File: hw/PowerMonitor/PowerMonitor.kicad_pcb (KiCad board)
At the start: 2 copper layers, 100 x 100 mm, 10 parts, among them J1 Conn_01x02_Socket, J2 Conn_01x02_Socket, J3 Conn_01x02_Socket, J4 Conn_01x02_Socket, J5 Conn_01x02_Socket

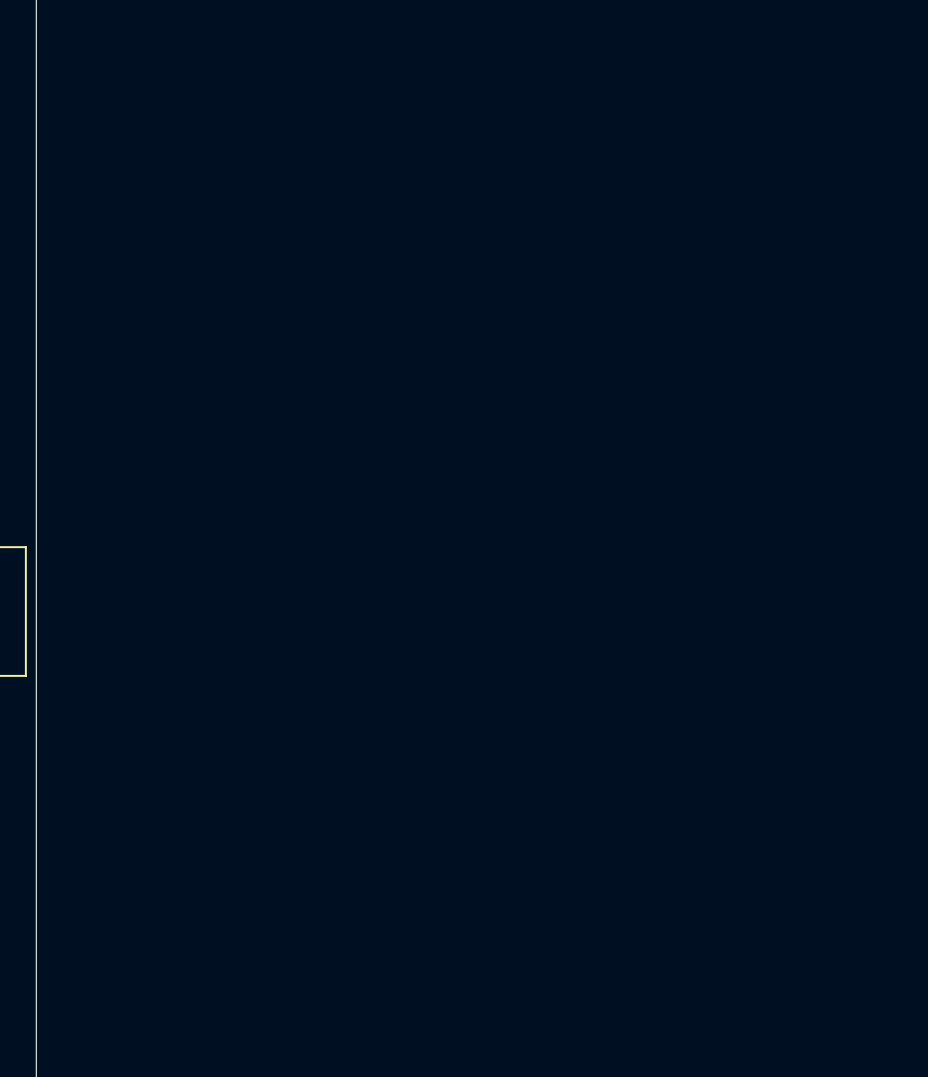
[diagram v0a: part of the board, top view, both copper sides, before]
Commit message: preliminar design for battery power monitor, add sd card to fmu
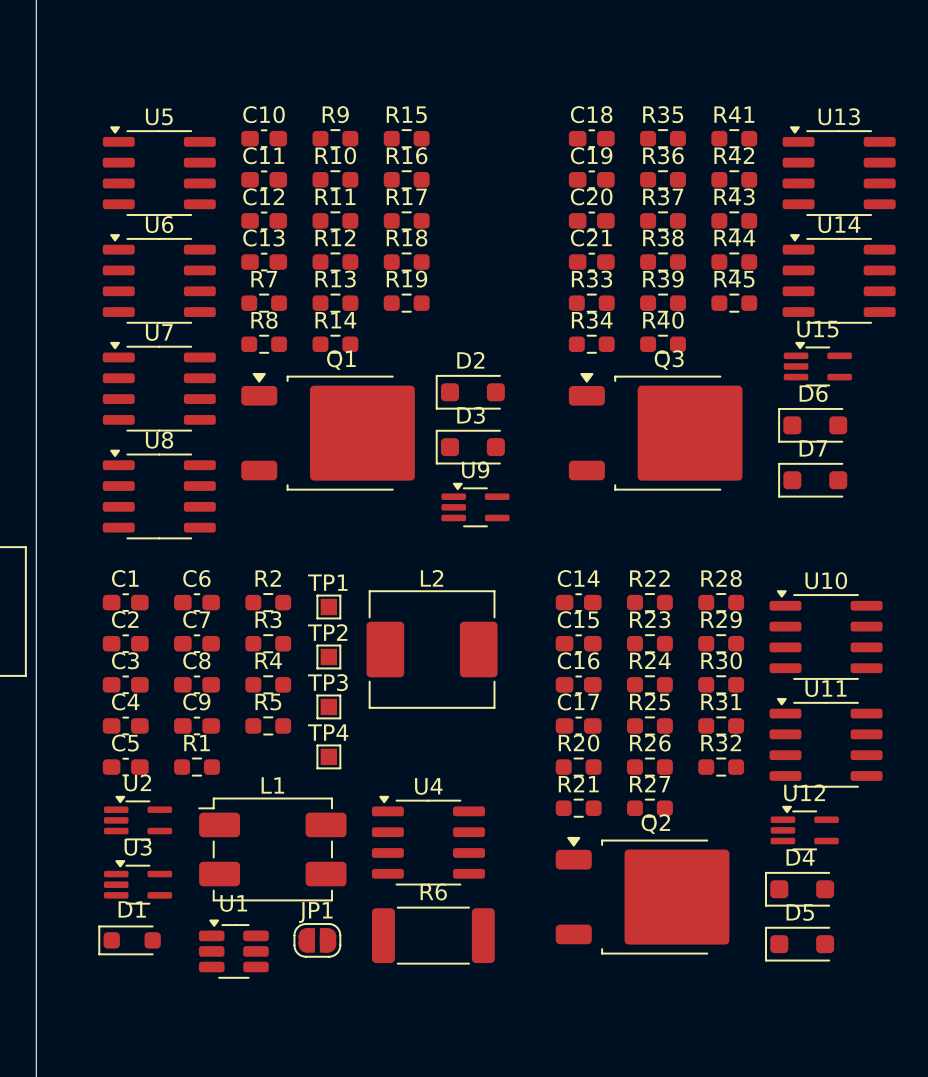
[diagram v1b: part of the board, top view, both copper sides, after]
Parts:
- added C1: 10 µF, Capacitor_SMD:C_0603_1608Metric_Pad1.08x0.95mm_HandSolder, F.Cu at (201.2, 90.2)
- added C10: 33n, Capacitor_SMD:C_0603_1608Metric_Pad1.08x0.95mm_HandSolder, F.Cu at (209.7, 61.8)
- added C11: 1u, Capacitor_SMD:C_0603_1608Metric_Pad1.08x0.95mm_HandSolder, F.Cu at (209.7, 64.3)
- added C12: 1u, Capacitor_SMD:C_0603_1608Metric_Pad1.08x0.95mm_HandSolder, F.Cu at (209.7, 66.8)
- added C13: 1u, Capacitor_SMD:C_0603_1608Metric_Pad1.08x0.95mm_HandSolder, F.Cu at (209.7, 69.4)
- added C14: 33n, Capacitor_SMD:C_0603_1608Metric_Pad1.08x0.95mm_HandSolder, F.Cu at (228.9, 90.2)
- added C15: 1u, Capacitor_SMD:C_0603_1608Metric_Pad1.08x0.95mm_HandSolder, F.Cu at (228.9, 92.7)
- added C16: 1u, Capacitor_SMD:C_0603_1608Metric_Pad1.08x0.95mm_HandSolder, F.Cu at (228.9, 95.2)
- added C17: 1u, Capacitor_SMD:C_0603_1608Metric_Pad1.08x0.95mm_HandSolder, F.Cu at (228.9, 97.7)
- added C18: 33n, Capacitor_SMD:C_0603_1608Metric_Pad1.08x0.95mm_HandSolder, F.Cu at (229.7, 61.8)
- added C19: 1u, Capacitor_SMD:C_0603_1608Metric_Pad1.08x0.95mm_HandSolder, F.Cu at (229.7, 64.3)
- added C2: 0.1 µF, Capacitor_SMD:C_0603_1608Metric_Pad1.08x0.95mm_HandSolder, F.Cu at (201.2, 92.7)
- added C20: 1u, Capacitor_SMD:C_0603_1608Metric_Pad1.08x0.95mm_HandSolder, F.Cu at (229.7, 66.8)
- added C21: 1u, Capacitor_SMD:C_0603_1608Metric_Pad1.08x0.95mm_HandSolder, F.Cu at (229.7, 69.4)
- added C3: 0.1 µF, Capacitor_SMD:C_0603_1608Metric_Pad1.08x0.95mm_HandSolder, F.Cu at (201.2, 95.2)
- added C4: 1u, Capacitor_SMD:C_0603_1608Metric_Pad1.08x0.95mm_HandSolder, F.Cu at (201.2, 97.7)
- added C5: 22 µF, Capacitor_SMD:C_0603_1608Metric_Pad1.08x0.95mm_HandSolder, F.Cu at (201.2, 100.2)
- added C6: 22 µF, Capacitor_SMD:C_0603_1608Metric_Pad1.08x0.95mm_HandSolder, F.Cu at (205.6, 90.2)
- added C7: 1u, Capacitor_SMD:C_0603_1608Metric_Pad1.08x0.95mm_HandSolder, F.Cu at (205.6, 92.7)
- added C8: 1u, Capacitor_SMD:C_0603_1608Metric_Pad1.08x0.95mm_HandSolder, F.Cu at (205.6, 95.2)
- added C9: C, Capacitor_SMD:C_0603_1608Metric_Pad1.08x0.95mm_HandSolder, F.Cu at (205.6, 97.7)
- added D1: PESD15VL1BA, Diode_SMD:D_SOD-323_HandSoldering, F.Cu at (201.6, 110.8)
- added D2: BZT52Bxx, Diode_SMD:D_SOD-123F, F.Cu at (222.4, 77.3)
- added D3: BZT52Bxx, Diode_SMD:D_SOD-123F, F.Cu at (222.4, 80.7)
- added D4: BZT52Bxx, Diode_SMD:D_SOD-123F, F.Cu at (242.5, 107.7)
- added D5: BZT52Bxx, Diode_SMD:D_SOD-123F, F.Cu at (242.5, 111.0)
- added D6: BZT52Bxx, Diode_SMD:D_SOD-123F, F.Cu at (243.3, 79.3)
- added D7: BZT52Bxx, Diode_SMD:D_SOD-123F, F.Cu at (243.3, 82.7)
- added JP1: SolderJumper_2_Open, Jumper:SolderJumper-2_P1.3mm_Open_RoundedPad1.0x1.5mm, F.Cu at (212.9, 110.8)
- added L1: L_Ferrite_Coupled_1423, Inductor_SMD:L_CommonModeChoke_TDK_ACM7060, F.Cu at (210.2, 105.2)
- added L2: KOHER_MDA7030 15uH, Inductor_SMD:L_KOHERelec_MDA7030, F.Cu at (219.9, 93.0)
- added Q1: Q_PMOS_GDS, Package_TO_SOT_SMD:TO-252-2, F.Cu at (214.4, 79.8)
- added Q2: Q_PMOS_GDS, Package_TO_SOT_SMD:TO-252-2, F.Cu at (233.6, 108.1)
- added Q3: Q_PMOS_GDS, Package_TO_SOT_SMD:TO-252-2, F.Cu at (234.4, 79.8)
- added R1: 0 ohm, Resistor_SMD:R_0603_1608Metric_Pad0.98x0.95mm_HandSolder, F.Cu at (205.6, 100.2)
- added R10: 1k, Resistor_SMD:R_0603_1608Metric_Pad0.98x0.95mm_HandSolder, F.Cu at (214.0, 64.3)
- added R11: 1k, Resistor_SMD:R_0603_1608Metric_Pad0.98x0.95mm_HandSolder, F.Cu at (214.0, 66.8)
- added R12: 5.6k, Resistor_SMD:R_0603_1608Metric_Pad0.98x0.95mm_HandSolder, F.Cu at (214.0, 69.4)
- added R13: 1.8k, Resistor_SMD:R_0603_1608Metric_Pad0.98x0.95mm_HandSolder, F.Cu at (214.0, 71.9)
- added R14: 150, Resistor_SMD:R_0603_1608Metric_Pad0.98x0.95mm_HandSolder, F.Cu at (214.0, 74.4)
- added R15: 150, Resistor_SMD:R_0603_1608Metric_Pad0.98x0.95mm_HandSolder, F.Cu at (218.4, 61.8)
- added R16: 16k, Resistor_SMD:R_0603_1608Metric_Pad0.98x0.95mm_HandSolder, F.Cu at (218.4, 64.3)
- added R17: 2k, Resistor_SMD:R_0603_1608Metric_Pad0.98x0.95mm_HandSolder, F.Cu at (218.4, 66.8)
- added R18: 4.7k, Resistor_SMD:R_0603_1608Metric_Pad0.98x0.95mm_HandSolder, F.Cu at (218.4, 69.4)
- added R19: 4.7k, Resistor_SMD:R_0603_1608Metric_Pad0.98x0.95mm_HandSolder, F.Cu at (218.4, 71.9)
- added R2: 100 kohm, Resistor_SMD:R_0603_1608Metric_Pad0.98x0.95mm_HandSolder, F.Cu at (209.9, 90.2)
- added R20: 1k, Resistor_SMD:R_0603_1608Metric_Pad0.98x0.95mm_HandSolder, F.Cu at (228.9, 100.2)
- added R21: 1k, Resistor_SMD:R_0603_1608Metric_Pad0.98x0.95mm_HandSolder, F.Cu at (228.9, 102.7)
- added R22: 1k, Resistor_SMD:R_0603_1608Metric_Pad0.98x0.95mm_HandSolder, F.Cu at (233.2, 90.2)
- added R23: 1k, Resistor_SMD:R_0603_1608Metric_Pad0.98x0.95mm_HandSolder, F.Cu at (233.2, 92.7)
- added R24: 1k, Resistor_SMD:R_0603_1608Metric_Pad0.98x0.95mm_HandSolder, F.Cu at (233.2, 95.2)
- added R25: 5.6k, Resistor_SMD:R_0603_1608Metric_Pad0.98x0.95mm_HandSolder, F.Cu at (233.2, 97.7)
- added R26: 1.8k, Resistor_SMD:R_0603_1608Metric_Pad0.98x0.95mm_HandSolder, F.Cu at (233.2, 100.2)
- added R27: 150, Resistor_SMD:R_0603_1608Metric_Pad0.98x0.95mm_HandSolder, F.Cu at (233.2, 102.7)
- added R28: 150, Resistor_SMD:R_0603_1608Metric_Pad0.98x0.95mm_HandSolder, F.Cu at (237.6, 90.2)
- added R29: 16k, Resistor_SMD:R_0603_1608Metric_Pad0.98x0.95mm_HandSolder, F.Cu at (237.6, 92.7)
- added R3: 22 kohm, Resistor_SMD:R_0603_1608Metric_Pad0.98x0.95mm_HandSolder, F.Cu at (209.9, 92.7)
- added R30: 2k, Resistor_SMD:R_0603_1608Metric_Pad0.98x0.95mm_HandSolder, F.Cu at (237.6, 95.2)
- added R31: 4.7k, Resistor_SMD:R_0603_1608Metric_Pad0.98x0.95mm_HandSolder, F.Cu at (237.6, 97.7)
- added R32: 4.7k, Resistor_SMD:R_0603_1608Metric_Pad0.98x0.95mm_HandSolder, F.Cu at (237.6, 100.2)
- added R33: 1k, Resistor_SMD:R_0603_1608Metric_Pad0.98x0.95mm_HandSolder, F.Cu at (229.7, 71.9)
- added R34: 1k, Resistor_SMD:R_0603_1608Metric_Pad0.98x0.95mm_HandSolder, F.Cu at (229.7, 74.4)
- added R35: 1k, Resistor_SMD:R_0603_1608Metric_Pad0.98x0.95mm_HandSolder, F.Cu at (234.0, 61.8)
- added R36: 1k, Resistor_SMD:R_0603_1608Metric_Pad0.98x0.95mm_HandSolder, F.Cu at (234.0, 64.3)
- added R37: 1k, Resistor_SMD:R_0603_1608Metric_Pad0.98x0.95mm_HandSolder, F.Cu at (234.0, 66.8)
- added R38: 5.6k, Resistor_SMD:R_0603_1608Metric_Pad0.98x0.95mm_HandSolder, F.Cu at (234.0, 69.4)
- added R39: 1.8k, Resistor_SMD:R_0603_1608Metric_Pad0.98x0.95mm_HandSolder, F.Cu at (234.0, 71.9)
- added R4: R, Resistor_SMD:R_0603_1608Metric_Pad0.98x0.95mm_HandSolder, F.Cu at (209.9, 95.2)
- added R40: 150, Resistor_SMD:R_0603_1608Metric_Pad0.98x0.95mm_HandSolder, F.Cu at (234.0, 74.4)
- added R41: 150, Resistor_SMD:R_0603_1608Metric_Pad0.98x0.95mm_HandSolder, F.Cu at (238.4, 61.8)
- added R42: 16k, Resistor_SMD:R_0603_1608Metric_Pad0.98x0.95mm_HandSolder, F.Cu at (238.4, 64.3)
- added R43: 2k, Resistor_SMD:R_0603_1608Metric_Pad0.98x0.95mm_HandSolder, F.Cu at (238.4, 66.8)
- added R44: 4.7k, Resistor_SMD:R_0603_1608Metric_Pad0.98x0.95mm_HandSolder, F.Cu at (238.4, 69.4)
- added R45: 4.7k, Resistor_SMD:R_0603_1608Metric_Pad0.98x0.95mm_HandSolder, F.Cu at (238.4, 71.9)
- added R5: R, Resistor_SMD:R_0603_1608Metric_Pad0.98x0.95mm_HandSolder, F.Cu at (209.9, 97.7)
- added R6: 1m, Resistor_SMD:R_2512_6332Metric_Pad1.40x3.35mm_HandSolder, F.Cu at (220.0, 110.5)
- added R7: 1k, Resistor_SMD:R_0603_1608Metric_Pad0.98x0.95mm_HandSolder, F.Cu at (209.7, 71.9)
- added R8: 1k, Resistor_SMD:R_0603_1608Metric_Pad0.98x0.95mm_HandSolder, F.Cu at (209.7, 74.4)
- added R9: 1k, Resistor_SMD:R_0603_1608Metric_Pad0.98x0.95mm_HandSolder, F.Cu at (214.0, 61.8)
- added TP1: TestPoint_Flag, TestPoint:TestPoint_Pad_1.0x1.0mm, F.Cu at (213.6, 90.4)
- added TP2: TestPoint_Flag, TestPoint:TestPoint_Pad_1.0x1.0mm, F.Cu at (213.6, 93.5)
- added TP3: TestPoint_Flag, TestPoint:TestPoint_Pad_1.0x1.0mm, F.Cu at (213.6, 96.5)
- added TP4: TestPoint_Flag, TestPoint:TestPoint_Pad_1.0x1.0mm, F.Cu at (213.6, 99.6)
- added U1: TPS54202DDC, Package_TO_SOT_SMD:SOT-23-6_Handsoldering, F.Cu at (207.8, 111.4)
- added U10: LM358, Package_SO:SOIC-8_3.9x4.9mm_P1.27mm, F.Cu at (244.0, 92.2)
- added U11: LM393, Package_SO:SOIC-8_3.9x4.9mm_P1.27mm, F.Cu at (244.0, 98.8)
- added U12: 74LVC1G32, Package_TO_SOT_SMD:SOT-353_SC-70-5_Handsoldering, F.Cu at (242.7, 104.1)
- added U13: LM358, Package_SO:SOIC-8_3.9x4.9mm_P1.27mm, F.Cu at (244.8, 63.9)
- added U14: LM393, Package_SO:SOIC-8_3.9x4.9mm_P1.27mm, F.Cu at (244.8, 70.5)
- added U15: 74LVC1G32, Package_TO_SOT_SMD:SOT-353_SC-70-5_Handsoldering, F.Cu at (243.5, 75.7)
- added U2: 74LVC1G32, Package_TO_SOT_SMD:SOT-353_SC-70-5_Handsoldering, F.Cu at (202.0, 103.4)
- added U3: 74LVC1G32, Package_TO_SOT_SMD:SOT-353_SC-70-5_Handsoldering, F.Cu at (202.0, 107.4)
- added U4: NE555D, Package_SO:SOIC-8_3.9x4.9mm_P1.27mm, F.Cu at (219.7, 104.8)
- added U5: LM358, Package_SO:SOIC-8_3.9x4.9mm_P1.27mm, F.Cu at (203.3, 63.9)
- added U6: LM358, Package_SO:SOIC-8_3.9x4.9mm_P1.27mm, F.Cu at (203.3, 70.5)
- added U7: LM358, Package_SO:SOIC-8_3.9x4.9mm_P1.27mm, F.Cu at (203.3, 77.1)
- added U8: LM393, Package_SO:SOIC-8_3.9x4.9mm_P1.27mm, F.Cu at (203.3, 83.7)
- added U9: 74LVC1G32, Package_TO_SOT_SMD:SOT-353_SC-70-5_Handsoldering, F.Cu at (222.6, 84.3)
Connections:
- BT1 pad 1: unconnected-(BT1-+-Pad1) -> /CellMonitor3/VbatH
- BT1 pad 2: unconnected-(BT1---Pad2) -> /CellMonitor2/Vprot
- BT2 pad 1: unconnected-(BT2-+-Pad1) -> /CellMonitor2/VbatH
- BT2 pad 2: unconnected-(BT2---Pad2) -> /CellMonitor1/Vprot
- BT3 pad 1: unconnected-(BT3-+-Pad1) -> /CellMonitor1/VbatH
- BT3 pad 2: unconnected-(BT3---Pad2) -> GNDREF
- J1 pad 1: unconnected-(J1-Pin_1-Pad1) -> VDC
- J1 pad 2: unconnected-(J1-Pin_2-Pad2) -> GNDREF
- J2 pad 1: unconnected-(J2-Pin_1-Pad1) -> VDC
- J2 pad 2: unconnected-(J2-Pin_2-Pad2) -> GNDREF
- J3 pad 1: unconnected-(J3-Pin_1-Pad1) -> VDC
- J3 pad 2: unconnected-(J3-Pin_2-Pad2) -> GNDREF
- J4 pad 1: unconnected-(J4-Pin_1-Pad1) -> VDC
- J4 pad 2: unconnected-(J4-Pin_2-Pad2) -> GNDREF
- J5 pad 1: unconnected-(J5-Pin_1-Pad1) -> VDC
- J5 pad 2: unconnected-(J5-Pin_2-Pad2) -> GNDREF
